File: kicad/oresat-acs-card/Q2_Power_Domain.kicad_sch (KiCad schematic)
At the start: 69 parts, among them Q21 MOSFET-PCH-SOT23-6, Q22 MOSFET-PCH-SOT23-6, Q23 PMV45EN2R, Q24 PMV45EN2R, Q25 MOSFET-PCH-dual-SOT23-6, U17 MAX7310ATE, U18 MAX4211FETE, U19 MIC842LYC5-TR, U20 MIC842LYC5-TR

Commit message: Updated ACS board. Changed mezzanine pinouts. Added 5 V supplies for each quadrant. Updated layout.
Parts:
- added C69: 10u, oresat-acs-card:.0805-B-NOSILK, symbol Device:C_Small
- added C74: 1u, Resistor_SMD:R_0603_1608Metric, symbol Device:C_Small
- added C75: 22u, Capacitor_SMD:C_1210_3225Metric, symbol Device:C_Small
- added C85: CL10B104KB8NNNL, oresat-acs-card:.0603-C-NOSILK, symbol oresat-acs-card-eagle-import:C-EU0603-C-NOSILK
- added D7: 150060VS55040, oresat-acs-card:LED-0603, symbol oresat-live-card-eagle-import:LED-GREEN0603
- added L2: 6.8u, oresat-acs-card:ECS-MPI4040, symbol oresat-live-card-eagle-import:L-ECS-MPI4040
- added R118, R119: RC0603FR-0710KL, oresat-acs-card:.0603-C-NOSILK, symbol oresat-acs-card-eagle-import:R-US_0603-C-NOSILK
- added R27, R31: 10k, Resistor_SMD:R_0603_1608Metric, symbol oresat-live-card-eagle-import:R-US_0603-A
- added TP76: TEST-POINT-LARGE-SQUARE, oresat-acs-card:1X01, symbol oresat-acs-card-eagle-import:TEST-POINT-LARGE-SQUARE
- added U34: TPS62112, oresat-acs-card:S-PVQFN-16, symbol oresat-live-card-eagle-import:TPS6211X
- added U39: TS5A21366DCUR, oresat-acs-card:DCU-R-PDSO-G8, symbol oresat-acs-card-eagle-import:TS5A21366DCUR
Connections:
- net GND: now also C69.2, C74.2, C75.2, C85.1, D7.C, U34.1 (GND), U34.11 (GND), U34.12 (GND), U34.16 (GND), U34.6 (LBO), U34.7 (LBI), U34.9 (GND), U34.PAD (GND), U39.4 (GND)
- net VBUSP_Q2: now also C69.1, C74.1, R27.2, U34.2 (VIN), U34.3 (VIN), U34.4 (EN), U34.8 (VIN)
- net VPD_Q2: now also C85.2, U39.8 (VCC)
- net at TP69.1, U17.12 (IO7): now also U39.3 (IN2), U39.7 (IN1)
- new net: D7.A, R31.1
- new net: R119.2, U39.5 (NO2)
- new net: L2.1, U34.14 (SW), U34.15 (SW)
- new net: R27.1, U34.5 (SYNC)
- new net: R118.2, U39.1 (NO1)
- new net 5V_Q2: C75.1, L2.2, R31.2, TP76.1, U34.10 (FB)
- new net C3-UART-RX: R118.1
- new net C3-UART-TX: R119.1
- new net UART_RX_Q2: U39.6 (COM2)
- new net UART_TX_Q2: U39.2 (COM1)
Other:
- note added: "0805"
- note added: "5V Card Switching Supply"

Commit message: Updated 5 V regulator and tweaked card layout. Cleaned up silkscreen layer and schematic.
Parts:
- removed L2: 6.8u, oresat-acs-card:ECS-MPI4040, symbol oresat-live-card-eagle-import:L-ECS-MPI4040
- removed R27, R31: 10k, Resistor_SMD:R_0603_1608Metric, symbol oresat-live-card-eagle-import:R-US_0603-A
- removed U34: TPS62112, oresat-acs-card:S-PVQFN-16, symbol oresat-live-card-eagle-import:TPS6211X
- added L2: 3u3, Inductor_SMD:L_Coilcraft_XxL4030, symbol Device:L_Small
- added R27, R28, R31: 100k, Resistor_SMD:R_0603_1608Metric, symbol Device:R_Small_US
- added U34: LTC3624, Package_DFN_QFN:DFN-8-1EP_3x3mm_P0.5mm_EP1.65x2.38mm, symbol U-Linear Tech-LTC3624:LTC3624
- C69: footprint oresat-acs-card:.0805-B-NOSILK -> Capacitor_SMD:C_0805_2012Metric; Distributor DigiKey -> (none); MPN CGA4J1X7R0J106M125AC -> (none)
- C74: value 1u -> 2u2; footprint Resistor_SMD:R_0603_1608Metric -> Capacitor_SMD:C_0603_1608Metric; Distributor DigiKey -> (none); MPN CGA3E1X7R1E105M080AE -> (none)
- C75: value 22u -> 47u; footprint Capacitor_SMD:C_1210_3225Metric -> Capacitor_SMD:C_1206_3216Metric; Distributor DigiKey -> (none); MFR (none) -> KYOCERA AVX; MPN CGA6P1X7R1C226M250AC -> 1206YD476MAT2A
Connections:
- net 5V_Q2: now also L2.2, R31.1, U34.5 (FB)
- net GND: now also R28.2, U34.8 (GND), U34.9 (GND)
- net VBUSP_Q2: now also U34.2 (Vin), U34.3 (RUN); no longer C74.1
- net at D7.A: now also R31.2
- new net: R27.2, R28.1, U34.7 (MODE)
- new net: L2.1, U34.1 (SW)
- new net: C74.1, R27.1, U34.6 (INTVcc)
- no-connect marks 0 -> 1
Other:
- note removed: "0805"
- moved on the sheet: C21, C22, C23, C24, C25, C85, D10, D7, D9, Q21A, Q22A, Q23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

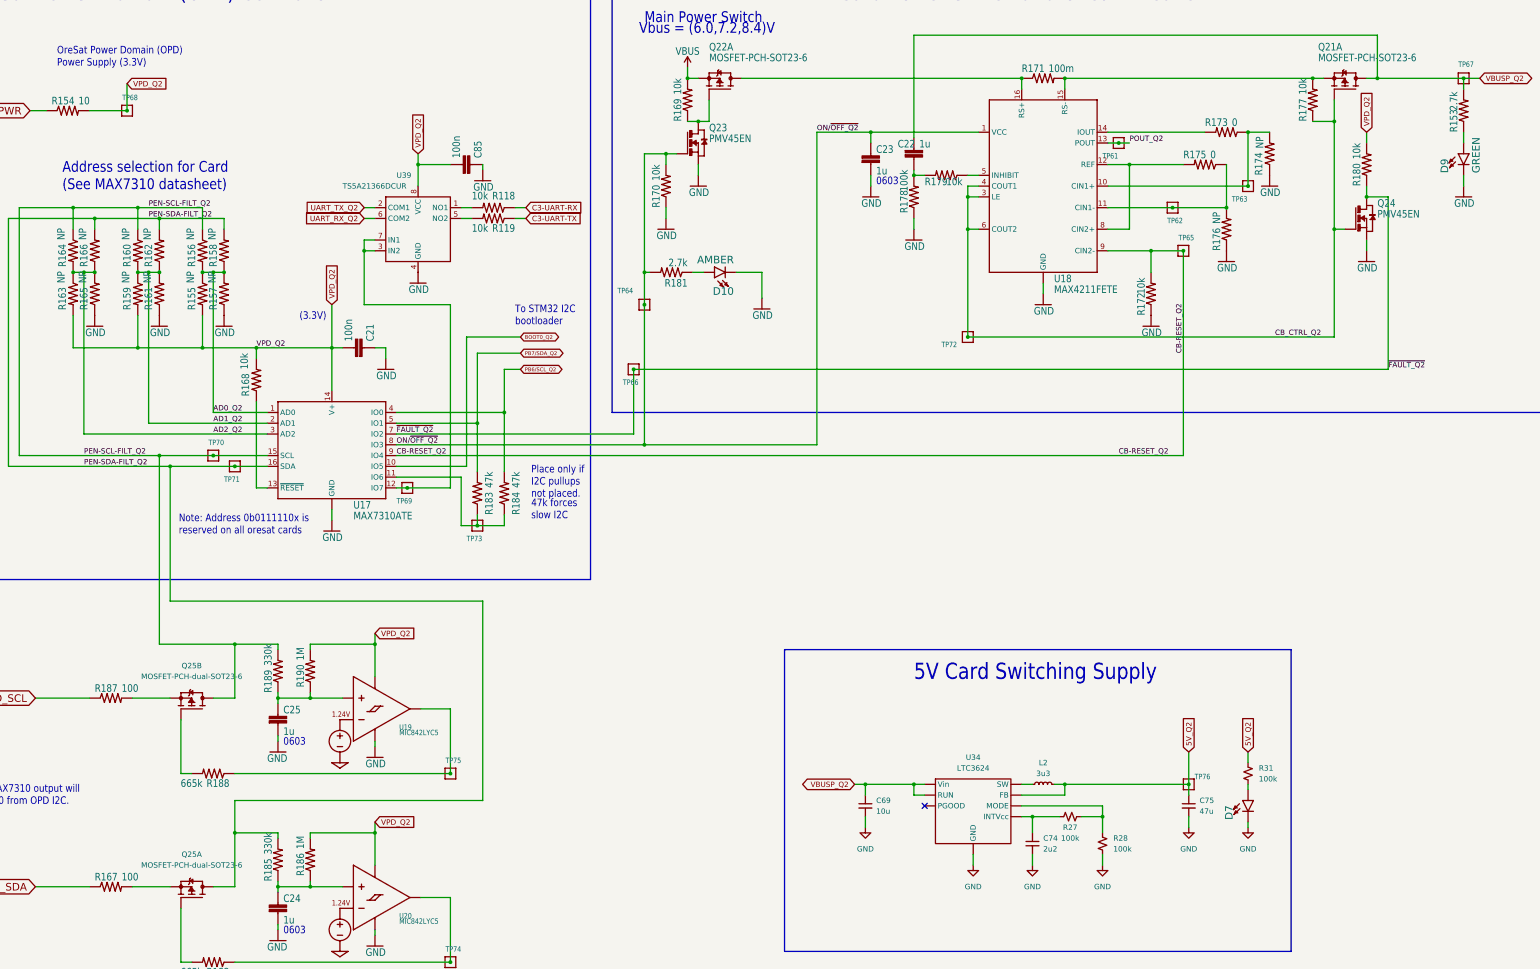
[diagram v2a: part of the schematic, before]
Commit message: Updated 5V regulators to match design block. Added UART switch to microcontroller. Added power flags and cleaned up ERC errors
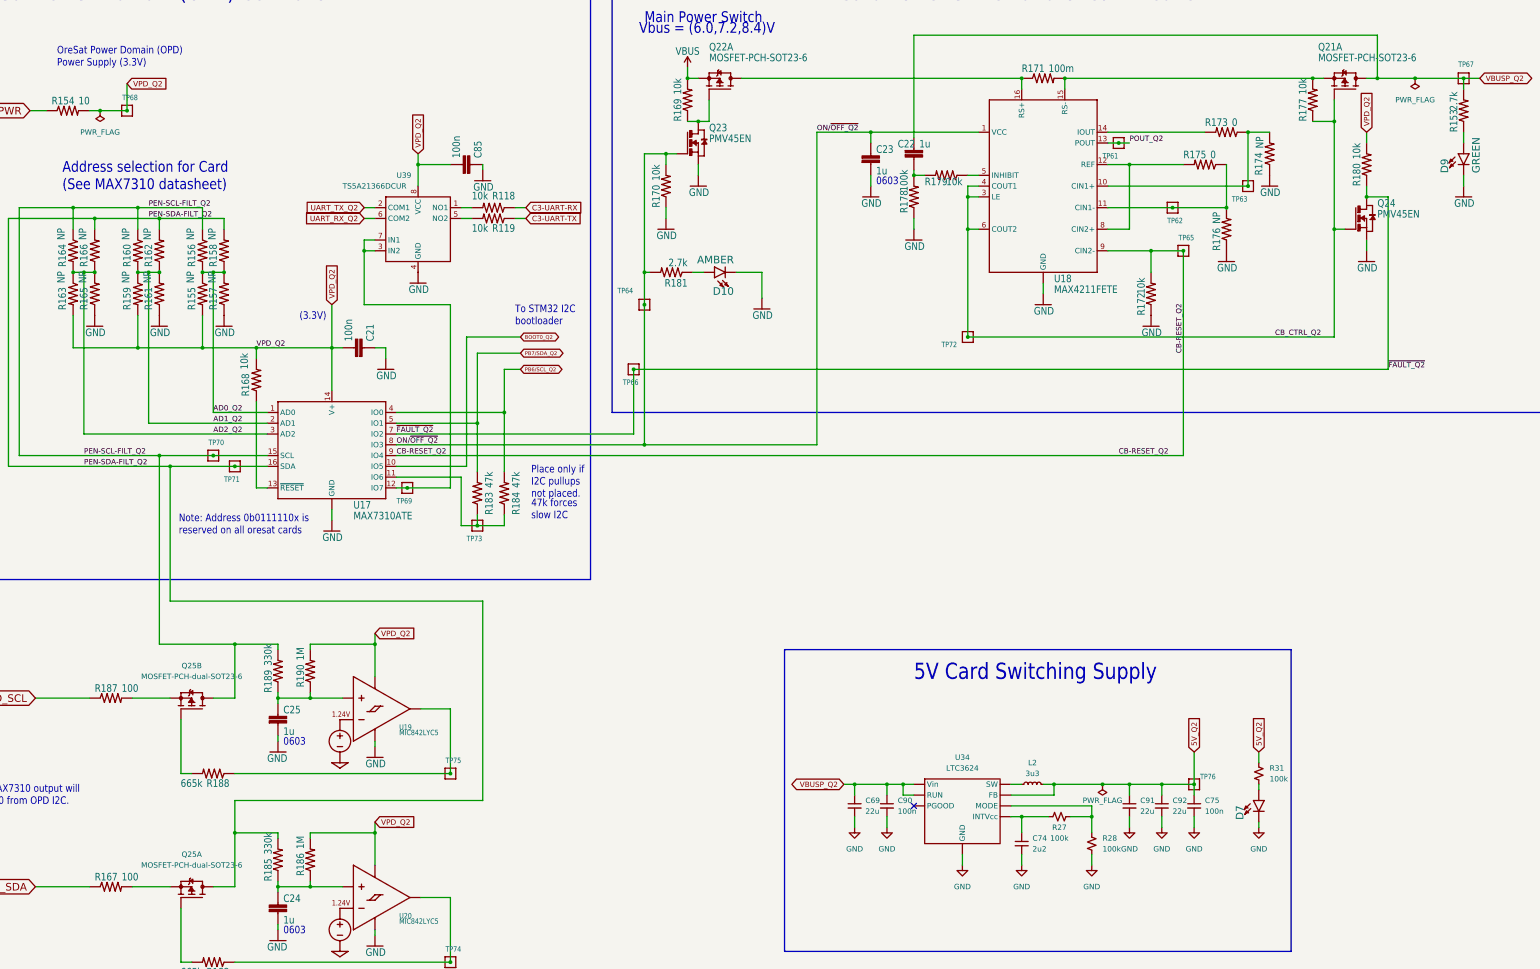
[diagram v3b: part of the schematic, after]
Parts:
- added C90: 100n, Capacitor_SMD:C_0603_1608Metric, symbol Device:C_Small
- added C91, C92: 22u, Capacitor_SMD:C_1210_3225Metric, symbol Device:C_Small
- C69: value 10u -> 22u; footprint Capacitor_SMD:C_0805_2012Metric -> Capacitor_SMD:C_1210_3225Metric
- C75: value 47u -> 100n; footprint Capacitor_SMD:C_1206_3216Metric -> Capacitor_SMD:C_0603_1608Metric
- D7: value 150060VS55040 -> LED-GREEN0603; symbol oresat-live-card-eagle-import:LED-GREEN0603 -> oresat-acs-card-eagle-import:LED-GREEN0603
- L2: footprint Inductor_SMD:L_Coilcraft_XxL4030 -> oresat-footprints:L_ECS-MPI4040
- U34: footprint Package_DFN_QFN:DFN-8-1EP_3x3mm_P0.5mm_EP1.65x2.38mm -> oresat-footprints:DFN-8-1EP_3x3mm_P0.5mm_EP1.65x2.38mm_ThermalVias0.3mm
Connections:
- net 5V_Q2: now also C91.1, C92.1
- net GND: now also C90.2, C91.2, C92.2
- net VBUSP_Q2: now also C90.1
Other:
- moved on the sheet: C69, C74, C75, D7, L2, R27, R28, R31, TP76, U34

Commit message: Design review changes.
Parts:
- R31: value 100k -> 10k
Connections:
- net VPD_Q2: no longer C85.2, U39.8 (VCC)
- net ON/~{OFF_Q2} renamed ON/~{OFF}_Q2
- net ON/~{OFF}_Q2: now also C85.2, U39.8 (VCC)
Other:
- note added: "Resistor values TBD"
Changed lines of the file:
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@@
   (junction (at 194.31 123.19) (diameter 0) (color 0 0 0 0)
+  )
+  (junction (at 194.31 54.61) (diameter 0) (color 0 0 0 0)
   )
   (junction (at 387.35 36.83) (diameter 0) (color 0 0 0 0)
@@
   )
   (wire (pts (xy 283.21 36.83) (xy 283.21 39.37))
+    (stroke (width 0) (type default) (color 0 0 0 0))
+  )
+  (wire (pts (xy 140.97 54.61) (xy 194.31 54.61))
     (stroke (width 0) (type default) (color 0 0 0 0))
   )
@@
     (effects (font (size 2.54 2.159)) (justify left bottom))
   )
+  (text "Resistor values TBD" (at 304.8 45.72 0)
+    (effects (font (size 1.27 1.27)) (justify left bottom))
+  )
   (text "OreSat Power Domain (OPD) Controller" (at 34.29 19.05 180)
     (effects (font (size 3.81 3.2385)) (justify left bottom))
@@
     (effects (font (size 1.2446 1.2446)) (justify left bottom))
   )
+  (label "ON{slash}~{OFF}_Q2" (at 140.97 54.61 0)
+    (effects (font (size 1.2446 1.2446)) (justify left bottom))
+  )
+  (label "ON{slash}~{OFF}_Q2" (at 194.31 67.31 90)
+    (effects (font (size 1.2446 1.2446)) (justify left bottom))
+  )
   (label "CB-RESET_Q2" (at 321.31 101.6 90)
     (effects (font (size 1.2446 1.2446)) (justify left bottom))
@@
     (effects (font (size 1.2446 1.2446)) (justify left bottom))
   )
-  (label "ON/~{OFF_Q2}" (at 135.89 123.19 0)
+  (label "ON{slash}~{OFF}_Q2" (at 135.89 123.19 0)
     (effects (font (size 1.2446 1.2446)) (justify left bottom))
   )
@@
     (effects (font (size 1.2446 1.2446)) (justify left bottom))
   )
-  (label "ON/~{OFF_Q2}" (at 234.95 49.53 0)
+  (label "ON/~{OFF}_Q2" (at 234.95 49.53 0)
     (effects (font (size 1.2446 1.2446)) (justify left bottom))
   )
@@
     )
   )
-  (global_label "VPD_Q2" (shape input) (at 140.97 54.61 90) (fields_autoplaced)
-    (effects (font (size 1.27 1.27)) (justify left))
-    (property "Intersheet References" "${INTERSHEET_REFS}" (id 0) (at 140.8906 45.0607 90)
-      (effects (font (size 1.27 1.27)) (justify left) hide)
-    )
-  )
   (global_label "UART_RX_Q2" (shape input) (at 128.27 69.85 180) (fields_autoplaced)
     (effects (font (size 1.27 1.27)) (justify right))
@@
       (effects (font (size 1.778 1.5113)) (justify left bottom))
     )
-    (property "Value" "2.7k" (id 1) (at 386.08 44.45 0)
+    (property "Value" "10k" (id 1) (at 386.08 44.45 0)
       (effects (font (size 1.778 1.5113)) (justify left bottom))
     )
@@
       (effects (font (size 1.27 1.27)) (justify left))
     )
-    (property "Value" "100k" (id 1) (at 341.63 201.9299 0)
+    (property "Value" "10k" (id 1) (at 341.63 201.9299 0)
       (effects (font (size 1.27 1.27)) (justify left))
     )
@@
       (effects (font (size 1.778 1.5113)) (justify left bottom))
     )
-    (property "Value" "2.7k" (id 1) (at 204.47 79.248 0)
+    (property "Value" "4.7k" (id 1) (at 204.47 79.248 0)
       (effects (font (size 1.778 1.5113)) (justify left bottom))
     )
@@
   (symbol (lib_id "oresat-acs-card-eagle-import:C-EU0603-C-NOSILK") (at 153.67 57.15 270) (mirror x) (unit 1)
     (in_bom yes) (on_board yes)
-    (property "Reference" "C85" (id 0) (at 154.051 55.626 0)
-      (effects (font (size 1.778 1.5113)) (justify left bottom))
-    )
-    (property "Value" "100n" (id 1) (at 148.971 55.626 0)
-      (effects (font (size 1.778 1.5113)) (justify left bottom))
-    )
+    (property "Reference" "C85" (id 0) (at 153.67 54.61 90)
+      (effects (font (size 1.778 1.5113)) (justify left bottom))
+    )
+    (property "Value" "100n" (id 1) (at 145.415 54.61 90)
+      (effects (font (size 1.778 1.5113)) (justify left bottom))
+    )
